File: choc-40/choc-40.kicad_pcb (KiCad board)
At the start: 2 copper layers, 222.6 x 76 mm, 103 parts, among them SW1 SW_Push, SW10 SW_Push, SW11 SW_Push, SW12 SW_Push, SW13 SW_Push, SW14 SW_Push, SW15 SW_Push, SW16 SW_Push, SW17 SW_Push, SW18 SW_Push, SW19 SW_Push, SW2 SW_Push, SW20 SW_Push, SW21 SW_Push, SW22 SW_Push, SW23 SW_Push, SW24 SW_Push, SW25 SW_Push, SW26 SW_Push, SW27 SW_Push, SW28 SW_Push, SW29 SW_Push, SW3 SW_Push, SW30 SW_Push, SW31 SW_Push, SW32 SW_Push, SW33 SW_Push, SW34 SW_Push, SW35 SW_Push, SW36 SW_Push, SW37 SW_Push, SW38 SW_Push, SW39 SW_Push, SW4 SW_Push, SW40 SW_Push, SW41 SW_Push, SW42 SW_Push, SW43 SW_Push, SW44 SW_Push, SW45 SW_Push, SW46 SW_Push, SW47 SW_Push, SW48 SW_Push, SW49 SW_Push, SW5 SW_Push, SW6 SW_Push, SW7 SW_Push, SW8 SW_Push, SW9 SW_Push, U2 ProMicro

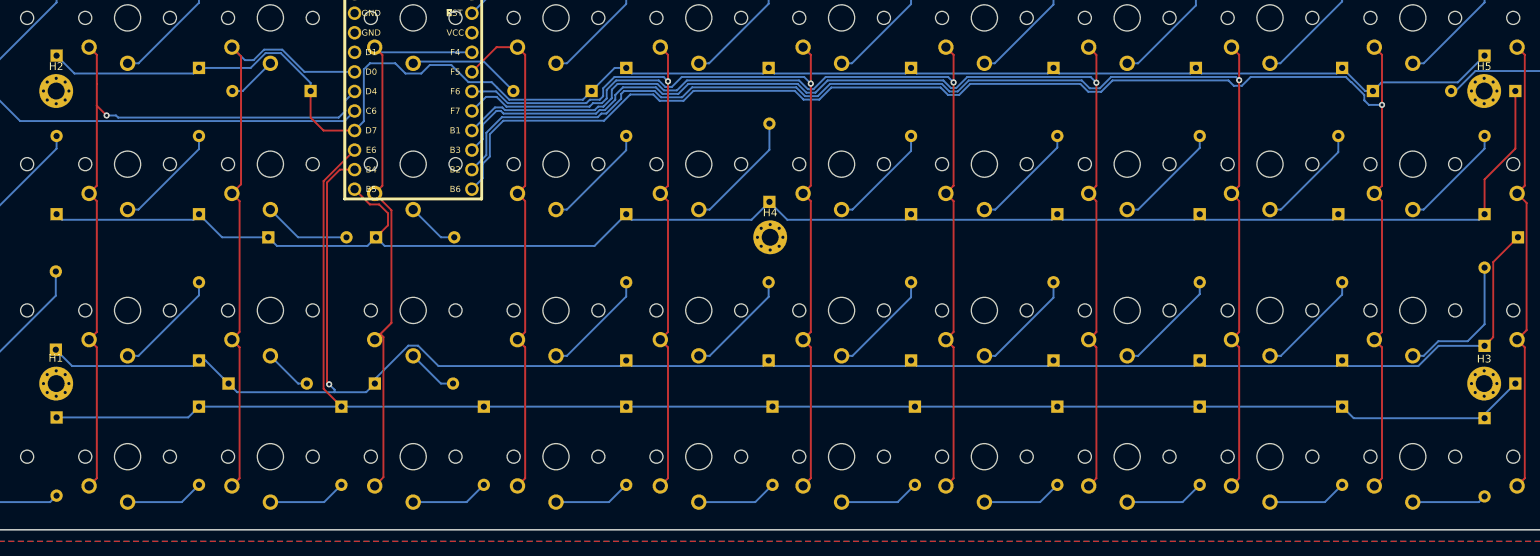
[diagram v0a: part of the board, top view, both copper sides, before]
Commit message: adding 2u middle key option
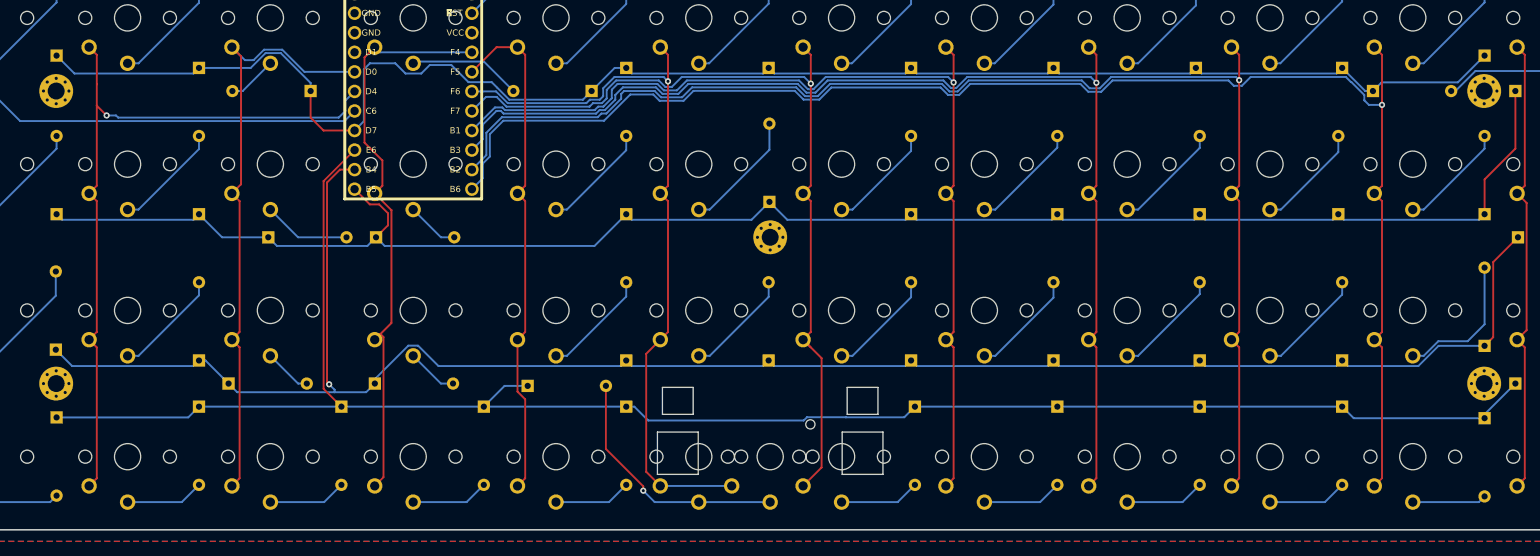
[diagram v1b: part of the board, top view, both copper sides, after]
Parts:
- added SW50: SW_Push, Keebio-Parts:Kailh-PG1350-2u-NoLED, F.Cu at (155.4, 123.2)
- H1, H2, H3, H4, H5: moved to B.Cu
- moved D24 31.9 mm to (123.9, 114.0), turned to 0 degrees
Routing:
- net Net-(D24-Pad2): track 10.5 -> 32.7 mm, vias 0 -> 1
- net COL6: track 87.8 -> 97.8 mm
- net ROW4: track 228.8 -> 237.1 mm
- net COL7: track 108.1 -> 110.7 mm
- net COL4: track 73.9 -> 75.0 mm

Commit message: adding base and plate
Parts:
- D1, D10, D11, D12, D13, D14, D15, D16, D17, D18, D19, D2, D20, D21, D22, D23, D24, D25, D26, D27, D28, D29, D3, D30, D31, D32, D33, D34, D35, D36, D37, D38, D39, D4, D40, D41, D42, D43, D44, D45, D46, D47, D48, D5, D6, D7, D8, D9: footprint Diode_THT:D_DO-35_SOD27_P10.16mm_Horizontal -> keyboard_parts:D_SOD123_axial
- U2: footprint Keebio-Parts:ArduinoProMicro -> Keebio-Parts:ArduinoProMicro-TopSide; moved to B.Cu
- moved SW25 42.9 mm to (79.8, 58.5)
- moved D9 19.9 mm to (75.9, 73.4)
- moved D13 19.2 mm to (113.1, 73.7)
- moved D1 15.8 mm to (48.1, 64.9)
- moved D41 15.8 mm to (233.6, 65.0)
- moved D43 15.8 mm to (233.6, 102.8)
- moved D22 15.8 mm to (140.8, 83.8)
- moved D5 15.8 mm to (66.6, 66.8)
- moved D7 15.8 mm to (66.6, 104.8)
- moved D37 15.7 mm to (215.1, 67.0)
- moved D2 15.7 mm to (48.1, 86.0)
- moved D30 15.7 mm to (178.1, 86.0)
- moved D34 15.7 mm to (196.6, 86.0)
- moved D35 15.7 mm to (196.6, 105.0)
- moved D39 15.7 mm to (215.1, 105.0)
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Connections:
- U2 pad 10: ROW4 -> COL9
- U2 pad 11: ROW3 -> COL10
- U2 pad 12: ROW2 -> COL11
- U2 pad 13: COL11 -> ROW2
- U2 pad 14: COL10 -> ROW3
- U2 pad 15: COL9 -> ROW4
- U2 pad 16: COL8 -> ROW1
- U2 pad 17: COL7 -> COL1
- U2 pad 18: COL6 -> COL2
- U2 pad 19: COL5 -> COL3
- U2 pad 20: COL4 -> (no net)
- U2 pad 5: (no net) -> COL5
- U2 pad 6: COL3 -> COL4
- U2 pad 7: COL2 -> COL6
- U2 pad 8: COL1 -> COL7
- U2 pad 9: ROW1 -> COL8
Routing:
- net ROW1: track 213.2 -> 199.7 mm
- net COL6: track 97.8 -> 87.3 mm
- net Net-(D24-Pad2): track 32.7 -> 24.8 mm, vias 1 -> 0
- net Net-(D10-Pad2): track 11.4 -> 4.52 mm
- net ROW3: track 244.9 -> 238.6 mm, vias 1 -> 0
- net Net-(D43-Pad2): track 18.4 -> 12.1 mm
- net ROW2: track 222.4 -> 217.1 mm
- net ROW4: track 237.1 -> 232.3 mm
- net COL7: track 110.7 -> 106.2 mm
- net COL4: track 75.0 -> 79.3 mm
- net Net-(D41-Pad2): track 15.9 -> 12.0 mm
- net COL11: track 192.3 -> 188.5 mm
- net Net-(D1-Pad2): track 15.9 -> 12.1 mm
- net Net-(D22-Pad2): track 15.8 -> 12.1 mm
- net Net-(D3-Pad2): track 15.6 -> 12.3 mm
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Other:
- board size 222.6 x 76 mm -> 223.1 x 76 mm

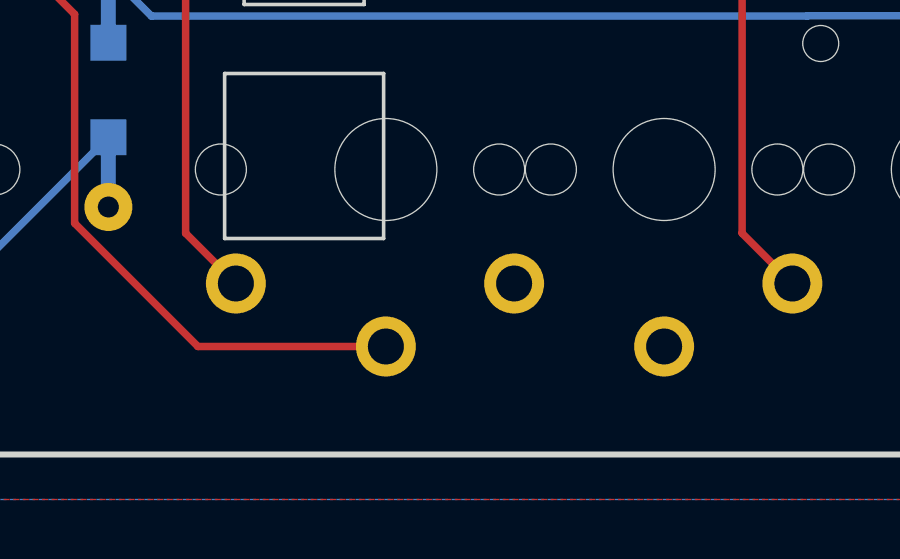
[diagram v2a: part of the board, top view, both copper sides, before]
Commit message: forgot to connect a trace
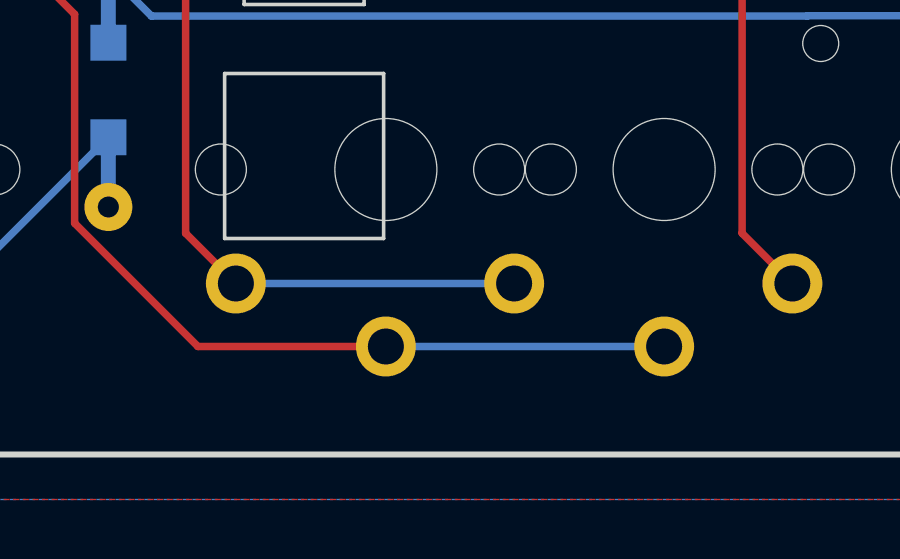
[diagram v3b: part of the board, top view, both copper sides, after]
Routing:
- net Net-(D24-Pad2): track 24.8 -> 34.1 mm
- net COL6: track 87.3 -> 96.6 mm

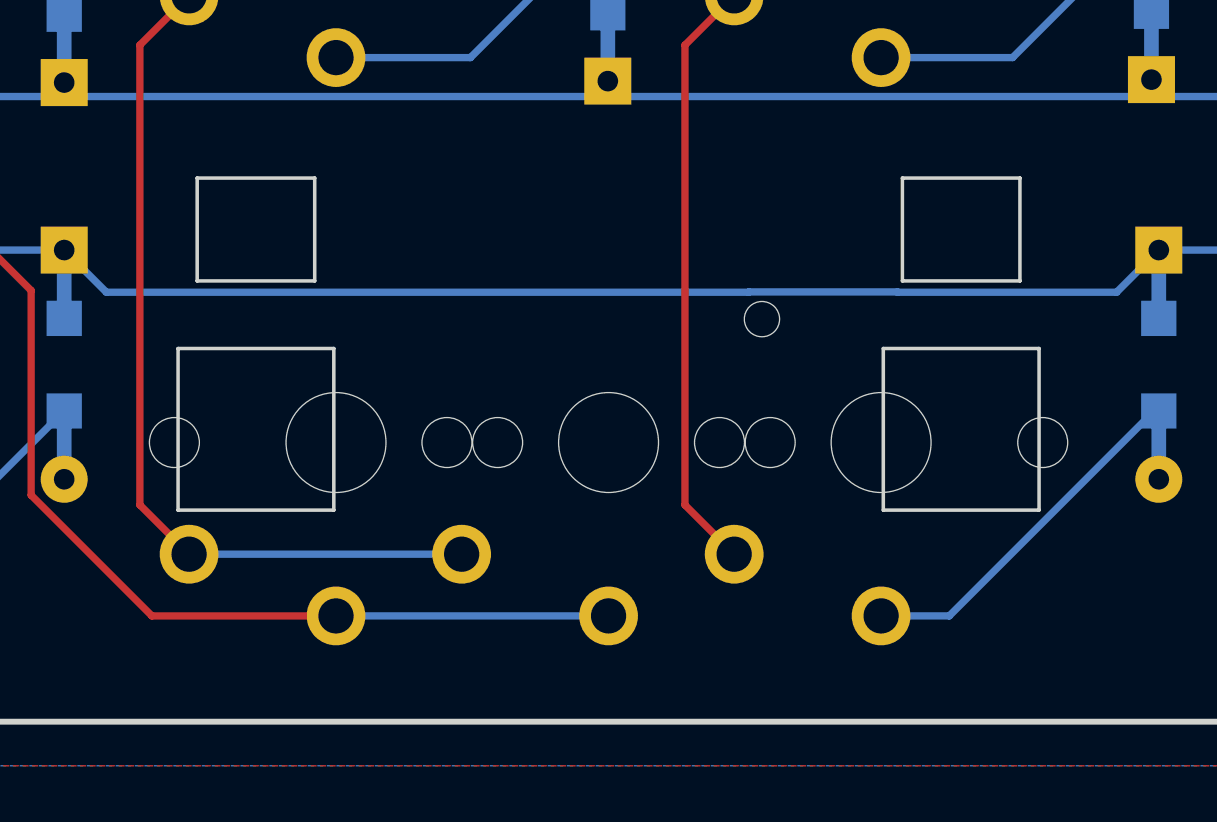
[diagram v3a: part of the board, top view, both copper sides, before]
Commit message: updating plate to 13.8x13.8mm
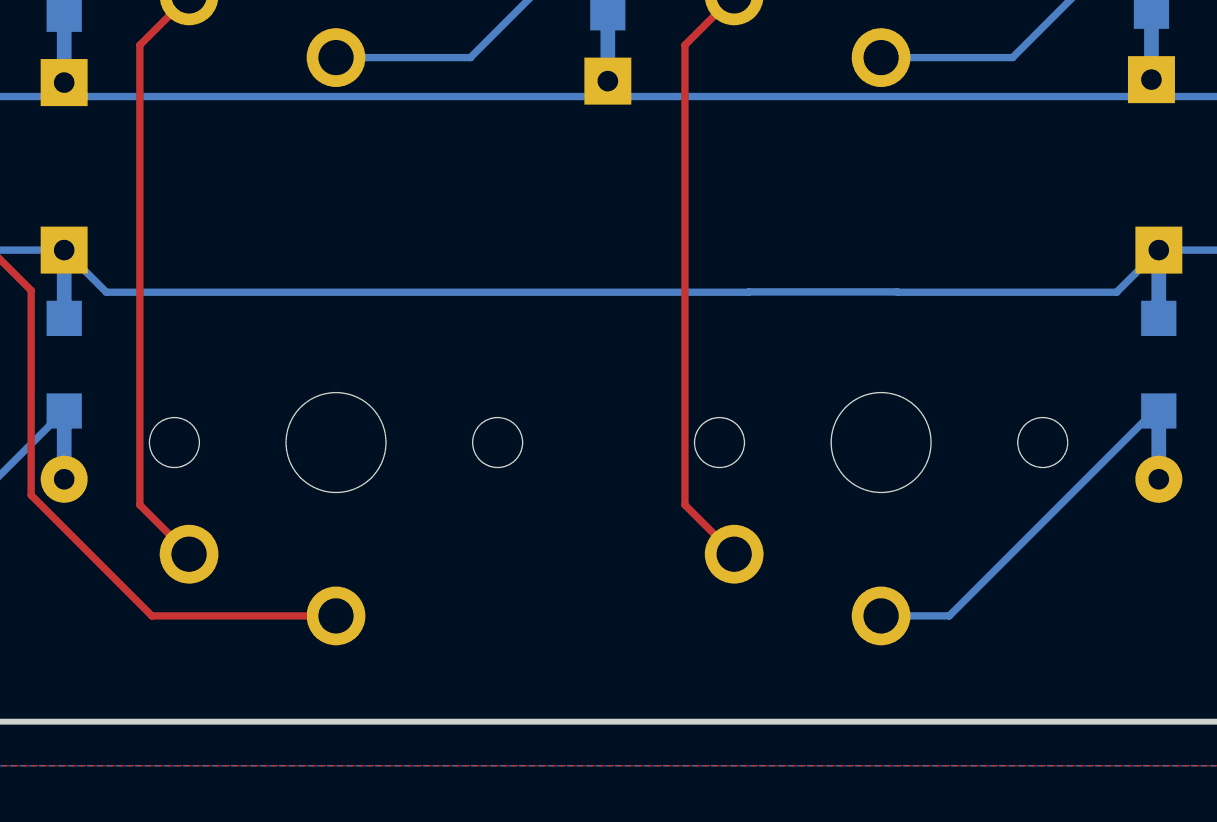
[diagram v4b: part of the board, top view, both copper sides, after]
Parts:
- removed SW50: SW_Push, Keebio-Parts:Kailh-PG1350-2u-NoLED
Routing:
- net Net-(D24-Pad2): track 34.1 -> 24.8 mm
- net COL6: track 96.6 -> 87.3 mm
